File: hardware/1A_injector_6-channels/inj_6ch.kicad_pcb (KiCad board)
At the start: 2 copper layers, 47.6 x 36.2 mm, 35 parts, among them P1 CONN_10X2, P2 CONN_2, P3 CONN_3, P4 CONN_2, P5 CONN_3, P7 CONN_10X2, Q1 OVP_DRIVER, Q2 OVP_DRIVER, Q3 OVP_DRIVER, Q4 OVP_DRIVER, Q5 OVP_DRIVER, Q6 OVP_DRIVER

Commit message: getting ready for Frankenstein
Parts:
- moved P2 98.1 mm to (222.4, 145.9)
- moved P3 98.1 mm to (222.4, 133.2)
- moved P4 98.1 mm to (222.4, 120.5)
- moved R18 98.1 mm to (198.2, 121.7)
- moved R7 98.1 mm to (194.8, 132.5)
- moved D1 98.1 mm to (201.4, 148.1)
- moved D4 98.1 mm to (214.2, 130.7)
- moved D5 98.1 mm to (214.2, 140.8)
- moved D7 98.1 mm to (214.2, 135.8)
- moved D8 98.1 mm to (215.9, 145.9)
- moved P5 98.1 mm to (189.4, 118.6)
- moved Q1 98.1 mm to (208.2, 140.7)
- moved Q2 98.1 mm to (201.9, 138.1)
- moved Q3 98.1 mm to (208.2, 133.0)
- moved Q4 98.1 mm to (201.9, 130.5)
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
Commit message: better design rules
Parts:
- moved P2 98.1 mm to (124.5, 151.1)
- moved P3 98.1 mm to (124.5, 138.4)
- moved P4 98.1 mm to (124.5, 125.7)
- moved R18 98.1 mm to (100.3, 126.9)
- moved R7 98.1 mm to (96.9, 137.7)
- moved D1 98.1 mm to (103.5, 153.3)
- moved D4 98.1 mm to (116.3, 135.9)
- moved D5 98.1 mm to (116.3, 146.1)
- moved D7 98.1 mm to (116.3, 141.0)
- moved D8 98.1 mm to (118.0, 151.1)
- moved P5 98.1 mm to (91.4, 123.8)
- moved Q1 98.1 mm to (110.3, 145.9)
- moved Q2 98.1 mm to (103.9, 143.3)
- moved Q3 98.1 mm to (110.3, 138.2)
- moved Q4 98.1 mm to (103.9, 135.7)
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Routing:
- net (no net): track 0.00 -> 31.9 mm, vias 0 -> 14
- net GND: track 303.5 -> 285.3 mm, vias 114 -> 97
- net /5V: track 78.1 -> 78.9 mm
- net /INJ-02_5V: track 18.0 -> 18.1 mm, vias 0 -> 1
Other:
- net class 1A EXT: clearance 0.1524 -> 0.254
- net class 5A EXT: clearance 0.1524 -> 0.254
- net class Default: clearance 0.1524 -> 0.254
- rule trace_clearance: 0.1524 -> 0.254
- board text added: "3V 5V GND"
- board text added: "DAECU rev A.02"
- board text added: "PB8 PE0 PE2 PE4 PE6 PC14 PH0 3V 5V GND"
- board text added: "PB9 PE1 PE3 PE5 PE13 PC15 PH1 3V 5V GND"
- board text added: "https://code.google.com/p/daecu/ for rusefi.com rev 0.1"
- board text removed: "DAECU"
- board text removed: "GND 5V 3V"
- board text removed: "https://code.google.com/p/daecu/ for rusefi.com rev 0.2"

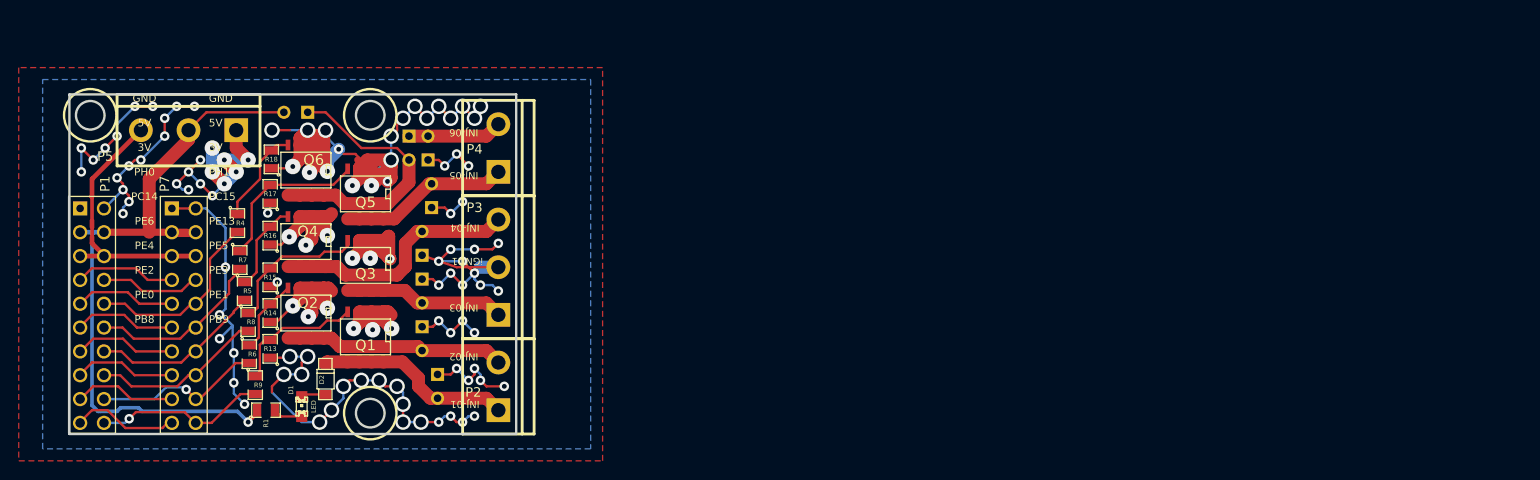
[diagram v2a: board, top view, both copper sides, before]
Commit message: move to better location
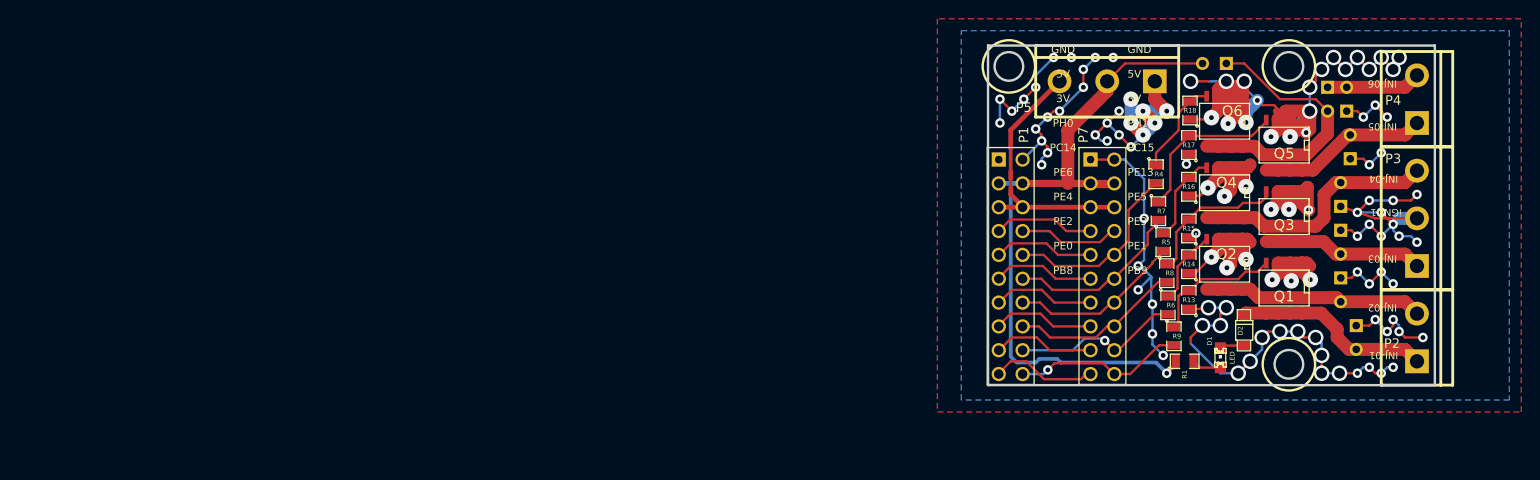
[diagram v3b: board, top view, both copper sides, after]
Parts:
- moved P2 98.1 mm to (222.4, 145.9)
- moved P3 98.1 mm to (222.4, 133.2)
- moved P4 98.1 mm to (222.4, 120.5)
- moved R18 98.1 mm to (198.2, 121.7)
- moved R7 98.1 mm to (194.8, 132.5)
- moved D1 98.1 mm to (201.4, 148.1)
- moved D4 98.1 mm to (214.2, 130.7)
- moved D5 98.1 mm to (214.2, 140.8)
- moved D7 98.1 mm to (214.2, 135.8)
- moved D8 98.1 mm to (215.9, 145.9)
- moved P5 98.1 mm to (189.4, 118.6)
- moved Q1 98.1 mm to (208.2, 140.7)
- moved Q2 98.1 mm to (201.9, 138.1)
- moved Q3 98.1 mm to (208.2, 133.0)
- moved Q4 98.1 mm to (201.9, 130.5)
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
